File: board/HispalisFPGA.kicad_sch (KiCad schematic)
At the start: 118 parts, among them J1 Conn_02x03_Odd_Even, J2 Conn_01x02_Socket, J3 USBC, SW1 SW_Push, SW2 SW_DIP_x08, U1 LFE5UM-285, U10 PUSB3FR4Z, U11 PUSB3FR4Z, U12 LTC-4627JR, U2 S27KS0641DPBHI020, U3 DSC6001CI2A-016.0000T, U4 FAN53555UC04X, U5 MIC5504-2.5YMT-TR, U6 Conn_02x03_Counter_Clockwise, U7 FAN53600, U8 S25FL064L, U9 MIC5504-1.2YMT-TR

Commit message: Re-annotate schematic and fix broken wires
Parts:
- C20: renamed from C12; value 10nf -> 10nF
- C21: renamed from C14; value 10nf -> 10nF
- C22: renamed from C16; value 10nf -> 10nF
- C23: renamed from C7; value 10nf -> 10nF
- C24: renamed from C31; value 10nf -> 10nF
- C25: renamed from C11; value 10nf -> 10nF
- C26: renamed from C35; value 10nf -> 10nF
- C27: renamed from C4; value 10nf -> 10nF
- R1: renamed from R10; value 4.7k -> 4.7K
- R2: renamed from R7; value 4.7k -> 4.7K
- R3: renamed from R5; value 4.7k -> 4.7K
- R4: value 4.7k -> 4.7K
- R7: renamed from R11; value 1.5k -> 1.5K
- renumbered U4 to 1V1_SW_REG1, U9 to 1V2_LDO_REG1, U5 to 2V5_LDO_REG1, U7 to 3V3_SW_REG1, J2 to 5V_LINE1, D1 to BLED1, D2 to BLED2, SW1 to BTN6, C10 to C1, C28 to C10, C44 to C11, C46 to C12, C45 to C13, C47 to C14, C39 to C15, C41 to C16, C24 to C17, C26 to C18, C18 to C19, C13 to C2, C8 to C28, C38 to C29, C15 to C3, C40 to C30, C17 to C31, C20 to C32, C42 to C33, C43 to C34, C5 to C35, C23 to C36, C36 to C37, C37 to C38, C19 to C39, C6 to C4, C22 to C40, C30 to C5, C9 to C6, C34 to C7, C3 to C8, C29 to C9, U12 to DISPLAY1, U2 to DRAM1, U10 to ESD1, U11 to ESD2, U8 to FLASH1, U1 to FPGA1, J1 to JTAG1, R17 to R10, R18 to R11, R19 to R12, R20 to R13, R21 to R14, R22 to R15, R1 to R16, R2 to R17, R6 to R18, R9 to R19, R14 to R20, R23 to R21, R24 to R22, R25 to R23, R26 to R24, R27 to R25, R28 to R26, R29 to R27, R30 to R28, R31 to R29, R32 to R30, R33 to R31, R34 to R32, R35 to R33, R36 to R34, R37 to R35, R38 to R36, R12 to R5, R13 to R6, R15 to R8, R16 to R9, SW2 to SW1, U3 to SYS_CLK1, TP12 to TP1, TP13 to TP2, TP1 to TP3, TP11 to TP4, J3 to USBC1
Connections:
- net +1V1: now also C1.1, C2.1, C20.1, C21.1, C22.1, C3.1, C40.1, L1.2
- net +1V2: now also C15.1, C16.1, C29.1, C30.1, C34.1, C37.1, C38.1
- net +2V5: now also C23.1, C32.1, C4.1
- net +3V3: now also C10.1, C17.1, C18.1, C19.1, C24.1, C25.1, C26.1, C27.1, C31.1, C33.1, C5.1, C6.1, C7.1, C8.1, C9.1, L2.2, R1.1, R3.1
- net +5V: now also C28.1, C35.1, C39.1
- net CFG_MODE_SEL_0: now also R2.1
- net CFG_MODE_SEL_1: now also R3.2
- net CH0_TXN: now also C14.2
- net CH0_TXP: now also C13.2
- net CH1_TXN: now also C12.1
- net CH1_TXP: now also C11.1
- net GND: now also C1.2, C10.2, C15.2, C16.2, C17.2, C18.2, C19.2, C2.2, C20.2, C21.2, C22.2, C23.2, C24.2, C25.2, C26.2, C27.2, C28.2, C29.2, C3.2, C30.2, C31.2, C32.2, C33.2, C34.2, C35.2, C36.2, C37.2, C38.2, C39.2, C4.2, C40.2, C5.2, C6.2, C7.2, C8.2, C9.2, R5.2, R6.2
- net PROGRAMN: now also R1.2
- net TCK: now also R4.1
- net USB_CONNECT: now also R7.1
- net USB_D+: now also R7.2
- net at L2.1: now also 3V3_SW_REG1.B1 (SW)
- net at 1V1_SW_REG1.D3 (SW[4]), 1V1_SW_REG1.D4 (SW[4]), 1V1_SW_REG1.E3 (SW[4])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: now also L1.1
- net at BLED1.1 (K): now also R5.1
- net at R6.1: now also BLED2.1 (K)
- net at C12.2: now also USBC1.A2 (TX1+)
- net at C11.2: now also USBC1.A3 (TX1-)
- net at C14.1: now also USBC1.B3 (TX2-)
- net at C13.1: now also USBC1.B2 (TX2+)
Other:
- moved on the sheet: BTN1, BTN2, BTN3, BTN4, BTN5, C11, C12, C13, C14, C36, LD1, LD2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

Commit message: Rearrange USB connections
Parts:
- removed USBC1: USBC, symbol HispalisFPGA:USBC-Components
- added USB_C1: USB_C_Receptacle, symbol Connector:USB_C_Receptacle
- R7: footprint Resistor_SMD:R_0402_1005Metric -> (none)
- renumbered ESD2 to ESD1, ESD1 to ESD2
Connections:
- net +5V: now also USB_C1.A4 (VBUS), USB_C1.A9 (VBUS), USB_C1.B4 (VBUS), USB_C1.B9 (VBUS)
- net CC1: now also USB_C1.A5 (CC1)
- net CC2: now also USB_C1.B5 (CC2)
- net GND: now also USB_C1.A1 (GND), USB_C1.A12 (GND), USB_C1.B1 (GND), USB_C1.B12 (GND)
- net SBU1: now also USB_C1.A8 (SBU1)
- net SBU2: now also USB_C1.B8 (SBU2)
- net USB_D+: now also FPGA1.F17 (PL29AB+/GR_PCLK6_0), USB_C1.A6 (D+), USB_C1.B6 (D+); no longer FPGA1.D16 (PL17AB-)
- net USB_D-: now also FPGA1.F16 (PL29AB-), USB_C1.A7 (D-), USB_C1.B7 (D-); no longer FPGA1.F17 (PL29AB+/GR_PCLK6_0)
- net at C12.2: now also USB_C1.A2 (TX1+)
- net at C11.2: now also USB_C1.A3 (TX1-)
- net at C14.1: now also USB_C1.B3 (TX2-)
- net at C13.1: now also USB_C1.B2 (TX2+)
- net CH0_RXN renamed CH1_RX+
- net CH1_RX+: now also FPGA1.V6 (HDRXP0_D0CH1), USB_C1.A11 (RX2+); no longer FPGA1.V8 (HDRXN0_D0CH0)
- net CH0_RXP renamed CH1_RX-
- net CH1_RX-: now also FPGA1.V5 (HDRXN0_D0CH1), USB_C1.A10 (RX2-); no longer FPGA1.V9 (HDRXP0_D0CH0)
- net CH0_TXN renamed CH0_RX+
- net CH0_RX+: now also FPGA1.V9 (HDRXP0_D0CH0), USB_C1.B11 (RX1+); no longer C14.2, FPGA1.V11 (HDTXN0_D0CH0)
- net CH0_TXP renamed CH0_RX-
- net CH0_RX-: now also FPGA1.V8 (HDRXN0_D0CH0), USB_C1.B10 (RX1-); no longer C13.2, FPGA1.V12 (HDTXP0_D0CH0)
- net CH1_RXN renamed CH0_TX+
- net CH0_TX+: now also C12.1, FPGA1.V12 (HDTXP0_D0CH0); no longer FPGA1.V5 (HDRXN0_D0CH1)
- net CH1_RXP renamed CH0_TX-
- net CH0_TX-: now also C11.1, FPGA1.V11 (HDTXN0_D0CH0); no longer FPGA1.V6 (HDRXP0_D0CH1)
- net CH1_TXN renamed CH1_TX+
- net CH1_TX+: now also C13.2, FPGA1.V3 (HDTXP0_D0CH1); no longer C12.1, FPGA1.V2 (HDTXN0_D0CH1)
- net CH1_TXP renamed CH1_TX-
- net CH1_TX-: now also C14.2, FPGA1.V2 (HDTXN0_D0CH1); no longer C11.1, FPGA1.V3 (HDTXP0_D0CH1)
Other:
- note removed: "Channel 1 polarity is inverted"
- moved on the sheet: C11, C12, C13, C14, ESD1, ESD2

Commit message: Fix power connections
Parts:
- removed 1V2_LDO_REG1: MIC5504-1.2YMT-TR, Package_DFN_QFN:UDFN-4-1EP_1x1mm_P0.65mm_EP0.48x0.48mm, symbol HispalisFPGA:MIC5504-1.8YM5-TR-Components
- removed C33, C34: 1uF, Capacitor_SMD:C_0402_1005Metric, symbol Device:C
- removed TP3: TEST, TestPoint:TestPoint_Pad_D1.0mm, symbol Connector:TestPoint
- renumbered C27 to C24, C24 to C25, C25 to C26, C26 to C27, C35 to C33, C36 to C34, C37 to C35, C38 to C36, C39 to C37, C40 to C38, C8 to C5, C5 to C6, C6 to C7, C7 to C8
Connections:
- net +1V2 is gone; now on net FPGA_PWR: C15.1, C16.1, C29.1, C30.1, C35.1, C36.1, FPGA1.P10 (VCCA0[2]), FPGA1.R10 (VCCA0[2]), FPGA1.T5 (VCCHTX1_D0CH1), FPGA1.U12 (VCCHTX0_D0CH0), FPGA1.U6 (VCCHRX1_D0CH1), FPGA1.U8 (VCCHRX0_D0CH0)
- net +1V1 renamed FPGA_PWR
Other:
- note added: "0 = 1.1 V 1 = 1.2 V"
- note added: "1.1/1.2 Volt Switching Regulator"
- note removed: "1.1 Volt Switching Regulator"
- note removed: "1.2 Volt LDO Regulator"
- note removed: "1.2v LDO is only used for boards with SERDES"
- moved on the sheet: 5V_LINE1, C24, C25, C26, C27, C5, C6, C7, C8, C9, DISPLAY1, R29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

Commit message: Check clocks
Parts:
- CLK2: renamed from U6; value Conn_02x03_Counter_Clockwise -> 200MHz
- renumbered SYS_CLK1 to CLK1
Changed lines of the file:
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@@
 		(on_board yes)
 		(dnp no)
-		(property "Reference" "SYS_CLK1"
+		(property "Reference" "CLK1"
 			(at 51.816 299.974 0)
 			(effects
@@
 			(project "HispalisFPGA"
 				(path "/864346d0-d3ef-428e-a44f-9476f195db98"
-					(reference "SYS_CLK1")
+					(reference "CLK1")
 					(unit 1)
 				)
@@
 		(on_board yes)
 		(dnp no)
-		(property "Reference" "U6"
+		(property "Reference" "CLK2"
 			(at 435.61 291.6682 0)
 			(effects
@@
 			)
 		)
-		(property "Value" "Conn_02x03_Counter_Clockwise"
+		(property "Value" "200MHz"
 			(at 435.61 293.9796 0)
 			(effects
@@
 			(project "HispalisFPGA"
 				(path "/864346d0-d3ef-428e-a44f-9476f195db98"
-					(reference "U6")
+					(reference "CLK2")
 					(unit 1)
 				)

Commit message: Component selection for assembly
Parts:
- added C39: 100nF, Capacitor_SMD:C_0402_1005Metric, symbol Device:C
- added C40: 10uF, Capacitor_SMD:C_0603_1608Metric, symbol Device:C
- added R37: 100R, Resistor_SMD:R_0402_1005Metric, symbol Device:R
- 1V1_SW_REG1: JLC (none) -> WLCSP-20(1.6x2); LCSC (none) -> C603207
- 2V5_LDO_REG1: value MIC5504-2.5YMT-TR -> TLV73325PDBVR; footprint Package_DFN_QFN:UDFN-4-1EP_1x1mm_P0.65mm_EP0.48x0.48mm -> Package_TO_SOT_SMD:SOT-23-5; symbol HispalisFPGA:MIC5504-2.5YM5-TR-Components -> Regulator_Linear:TLV73325PDBV; JLC (none) -> SOT-23-5; LCSC (none) -> C882825
- 3V3_SW_REG1: value FAN53600 -> TPS63001DRCR; footprint Footprints:WLCSP-6 -> Package_SON:Texas_DRC0010J_ThermalVias; symbol HispalisFPGA:FAN53600-Components -> Regulator_Switching:TPS63001; JLC (none) -> VSON-10-EP(3x3); LCSC (none) -> C28060
- 5V_LINE1: JLC (none) -> Plugin,P=2.54mm; LCSC (none) -> C49661
- BLED1, BLED2: JLC (none) -> 0603; LCSC (none) -> C2286
- BTN1, BTN2, BTN3, BTN4, BTN5, BTN6: JLC (none) -> Plugin,6x6mm; LCSC (none) -> C7542846
- C1, C10, C11, C12, C13, C14, C15, C16, C17, C18, C19, C2, C3, C4, C5, C6, C7, C8, C9: JLC (none) -> 0402; LCSC (none) -> C1525
- C20, C21, C22, C23, C24, C25, C26, C27, C28, C29, C30: JLC (none) -> 0402; LCSC (none) -> C15195
- C31, C32: JLC (none) -> 0402; LCSC (none) -> C52923
- C33, C34: JLC (none) -> 0603; LCSC (none) -> C19702
- C35, C36: JLC (none) -> 0402; LCSC (none) -> C1523
- C37: value 2.2uF -> 10uF; footprint Capacitor_SMD:C_0402_1005Metric -> Capacitor_SMD:C_0603_1608Metric; JLC (none) -> 0603; LCSC (none) -> C19702
- C38: JLC (none) -> 0603; LCSC (none) -> C59461
- CLK1: value DSC6001CI2A-016.0000T -> ASEDV-16.000MHZ-LR-T; footprint Footprints:CDFN3225-4LD-PL-1 -> Oscillator:Oscillator_SMD_Abracon_ASE-4Pin_3.2x2.5mm; symbol HispalisFPGA:DSC6001CI2A-016.0000T-Components -> Oscillator:ASE-xxxMHz; JLC (none) -> SMD3225-4P; LCSC (none) -> C1857764
- CLK2: value 200MHz -> SWPM201DCAIAB-200.000000; footprint (none) -> Oscillator:Oscillator_SMD_SiTime_PQFD-6L_3.2x2.5mm; symbol Connector_Generic:Conn_02x03_Counter_Clockwise -> Oscillator:SiT9365xx-xBx-xxE; JLC (none) -> SMD3225-6P; LCSC (none) -> C5128599
- DISPLAY1: value LTC-4627JR -> SR410361N; JLC (none) -> Plugin; LCSC (none) -> C132660
- DRAM1: JLC (none) -> VBGA-24; LCSC (none) -> C2948494
- ESD1, ESD2: JLC (none) -> DFN2510A-10; LCSC (none) -> C503418
- FLASH1: footprint Footprints:UNF008 -> Package_SO:SOIC-8_5.275x5.275mm_P1.27mm; JLC (none) -> SOIC-8-208mil; LCSC (none) -> C2909898
- FPGA1: JLC (none) -> CSFBGA-285; LCSC (none) -> C1552182
- JTAG1: footprint (none) -> Connector_PinSocket_2.54mm:PinSocket_2x03_P2.54mm_Vertical_SMD; JLC (none) -> Plugin,P=2.54mm; LCSC (none) -> C5116527
- L1: footprint Inductor_SMD:L_2512_6332Metric -> Inductor_SMD:L_1008_2520Metric; JLC (none) -> 1008; LCSC (none) -> C375957
- L2: value 1uH -> 2.2uH; footprint Inductor_SMD:L_2010_5025Metric -> Inductor_SMD:L_0805_2012Metric; JLC (none) -> 0805; LCSC (none) -> C2049745
- LD1, LD2, LD3, LD4, LD5, LD6, LD7, LD8: JLC (none) -> 0805; LCSC (none) -> C2297
- PMOD1, PMOD2, PMOD3, PMOD4: JLC (none) -> Push-Pull,P=2.5mm; LCSC (none) -> C5333437
- R1, R2, R3, R4, R5, R6: JLC (none) -> 0402; LCSC (none) -> C25900
- R10, R11, R12, R13, R14, R15, R16, R17, R18, R19, R20, R8, R9: JLC (none) -> 0402; LCSC (none) -> C25744
- R21, R22, R23, R24, R25, R26, R27, R28: JLC (none) -> 0402; LCSC (none) -> C25087
- R29, R30, R31, R32, R33, R34, R35, R36: value 500R -> 1K; JLC (none) -> 0402; LCSC (none) -> C11702
- R7: footprint (none) -> Resistor_SMD:R_0402_1005Metric; JLC (none) -> 0402; LCSC (none) -> C25867
- SW1: footprint Button_Switch_SMD:SW_DIP_SPSTx04_Slide_6.7x11.72mm_W6.73mm_P2.54mm_LowProfile_JPin -> Button_Switch_SMD:SW_DIP_SPSTx08_Slide_6.7x21.88mm_W6.73mm_P2.54mm_LowProfile_JPin; JLC (none) -> SMD; LCSC (none) -> C5439774
- USB_C1: footprint (none) -> Connector_USB:USB_C_Receptacle_CNCTech_C-ARA1-AK51X; JLC (none) -> SMD; LCSC (none) -> C2927039
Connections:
- net +2V5: now also 2V5_LDO_REG1.5 (OUT); no longer 2V5_LDO_REG1.1 (VOUT)
- net +3V3: now also 3V3_SW_REG1.1 (VOUT), 3V3_SW_REG1.10 (FB), C40.1; no longer 2V5_LDO_REG1.3 (EN), 2V5_LDO_REG1.4 (VIN), 3V3_SW_REG1.C1 (FB), C31.1, L2.2
- net +5V: now also 2V5_LDO_REG1.1 (IN), 2V5_LDO_REG1.3 (EN), 3V3_SW_REG1.5 (VIN), C31.1, R37.1; no longer 3V3_SW_REG1.A2 (VIN), 3V3_SW_REG1.B2 (EN)
- net GND: now also 3V3_SW_REG1.11 (PGND), 3V3_SW_REG1.3 (PGND), 3V3_SW_REG1.9 (GND), C39.1, C40.2; no longer 3V3_SW_REG1.A1 (MODE), 3V3_SW_REG1.C2 (GND)
- net at L2.1: now also 3V3_SW_REG1.2 (L2); no longer 3V3_SW_REG1.B1 (SW)
- net USB3_REFCLK_0 renamed USB3_REFCLK_P
- net USB3_REFCLK_1 renamed USB3_REFCLK_N
- new net: 3V3_SW_REG1.4 (L1), L2.2
- new net: 3V3_SW_REG1.6 (EN), 3V3_SW_REG1.7 (PS/SYNC), 3V3_SW_REG1.8 (VINA), C39.2, R37.2
- no-connect marks 2 -> 1
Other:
- moved on the sheet: C19, C31, C32, C34, C37, C9, L2, TP2

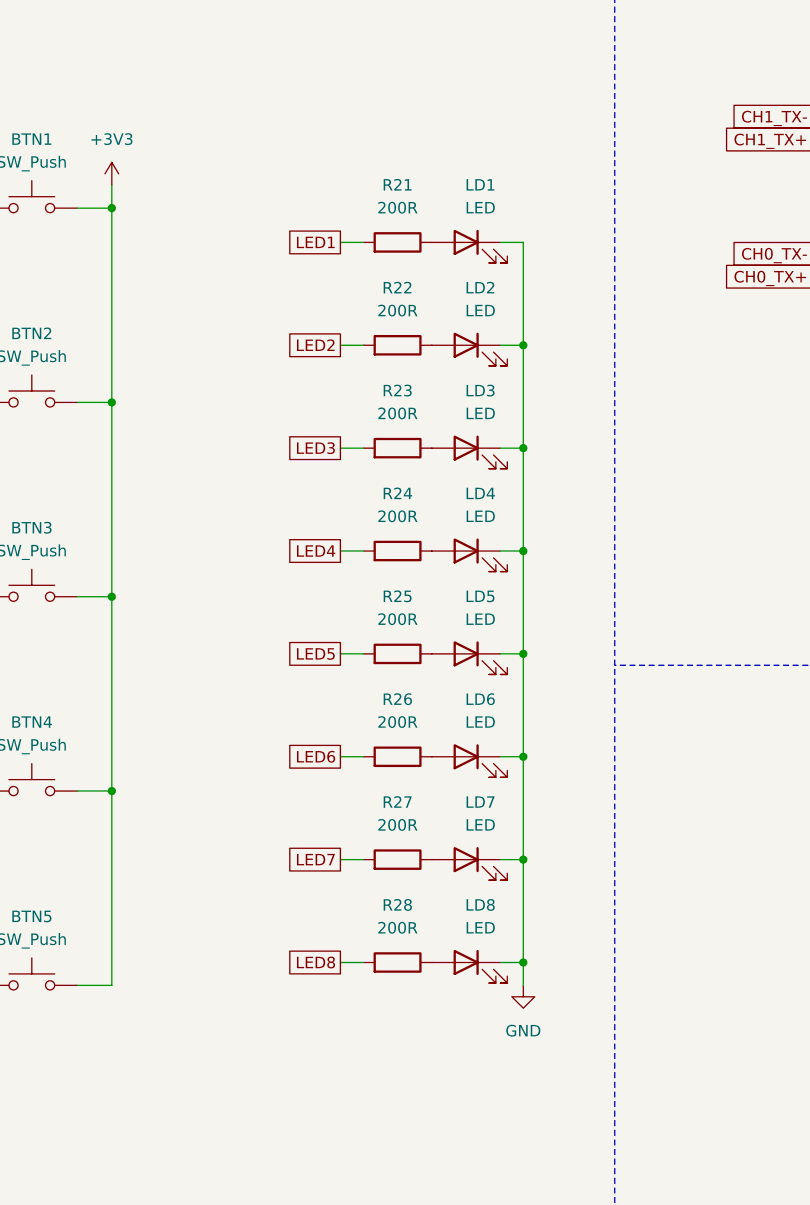
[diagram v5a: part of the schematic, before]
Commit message: Remove unnecessary resistors for LEDs
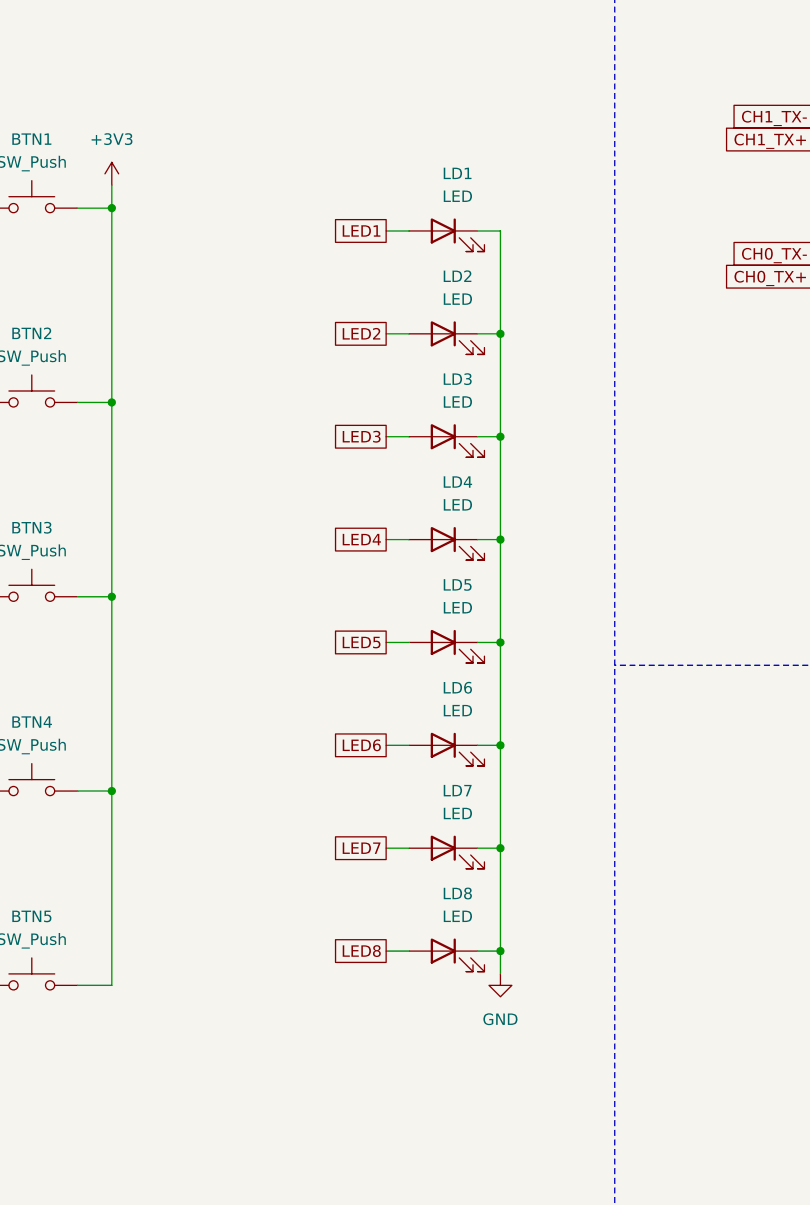
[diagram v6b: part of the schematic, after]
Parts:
- removed R21, R22, R23, R24, R25, R26, R27, R28: 200R, Resistor_SMD:R_0402_1005Metric, symbol Device:R
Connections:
- net LED1: now also LD1.2 (A)
- net LED2: now also LD2.2 (A)
- net LED3: now also LD3.2 (A)
- net LED4: now also LD4.2 (A)
- net LED5: now also LD5.2 (A)
- net LED6: now also LD6.2 (A)
- net LED7: now also LD7.2 (A)
- net LED8: now also LD8.2 (A)
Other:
- moved on the sheet: LD1, LD2, LD3, LD4, LD5, LD6, LD7, LD8
